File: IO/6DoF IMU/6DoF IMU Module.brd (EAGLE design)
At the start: 25.4 x 25.4 mm, 18 parts, among them U1 MPU-6050

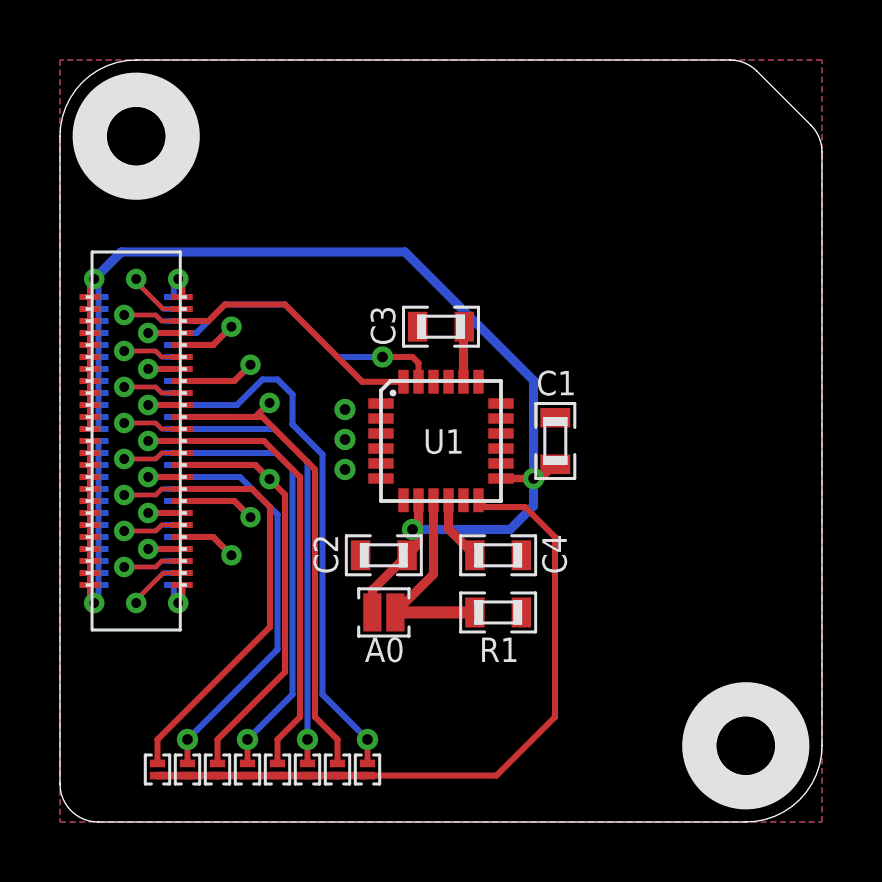
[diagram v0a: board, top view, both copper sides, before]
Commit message: Updated 6DoF IMU Module silkscreen and connections.
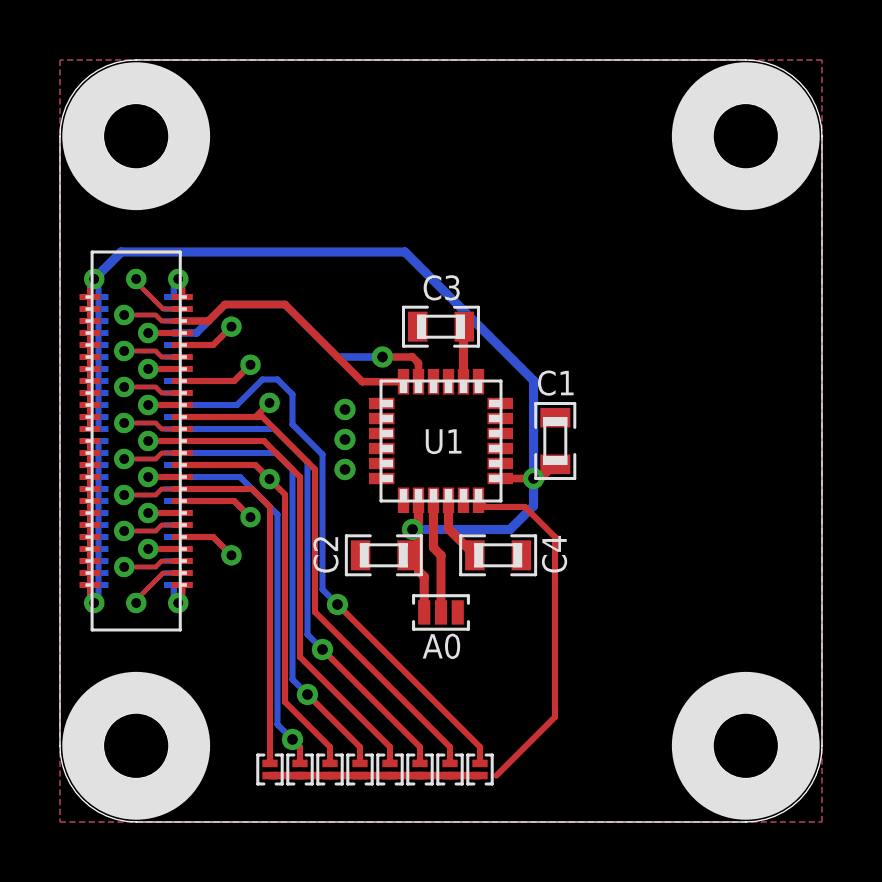
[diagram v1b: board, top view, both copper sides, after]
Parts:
- removed R1: 100k, .standardparts:0603
- added U$12, U$2: HOLE.#2, .screw_holes:#2
- A0: device .solderjumper:2.LRG -> .solderjumper:3.MED.23
- U$3, U$4: value HOLE.2MM -> HOLE.#2; device .screw_holes:2MM -> .screw_holes:#2
- U1: device invensense:QFN -> invensense:QFN.24.4X4
- moved J1 3.75 mm to (14.0, 1.75)
- moved J2 3.75 mm to (13.0, 1.75)
- moved J3 3.75 mm to (12.0, 1.75)
- moved J4 3.75 mm to (11.0, 1.75)
- moved J5 3.75 mm to (10.0, 1.75)
- moved J6 3.75 mm to (9.00, 1.75)
- moved J7 3.75 mm to (8.00, 1.75)
- moved J8 3.75 mm to (7.00, 1.75)
- moved A0 1.90 mm to (12.7, 6.99)
- turned C3 to 180 degrees
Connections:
- removed net N$16: C3.2, U1.20
- new net N$27: C3.1, U1.20
- net GND: now also A0.3, C3.2, U1.11; no longer C3.1, R1.2
- net N$18: no longer R1.1
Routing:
- net INT: track 23.1 -> 18.8 mm
- net N$18: track 6.92 -> 3.84 mm
- net N$27: track 0.00 -> 1.85 mm
- net N$16: track 1.85 -> 0.00 mm
- net N$26: track 13.3 -> 11.7 mm
- net N$21: track 15.0 -> 16.5 mm
- net N$19: track 12.8 -> 14.4 mm
- net N$3: track 17.8 -> 19.4 mm
- net 3.3V: track 31.9 -> 33.4 mm
- net N$25: track 13.5 -> 12.6 mm
- net N$22: track 14.3 -> 15.2 mm
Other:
- outline, holes or cut-outs redrawn
- board text added: "1"
- board text added: "8"
- board text added: "AnomalousMaker.com"
- board text removed: "InnovativeMaker.com"
